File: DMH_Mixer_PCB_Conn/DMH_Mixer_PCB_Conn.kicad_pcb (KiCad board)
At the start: 2 copper layers, 48 x 43 mm, 8 parts, among them J1 TS_Jack_6.35mm_Sw, J2 TS_Jack_6.35mm_Sw, J3 TS_Jack_6.35mm_Sw, J4 TS_Jack_6.35mm_Sw, J5 TS_Jack_6.35mm_Sw, J50 Conn_01x08, J6 TS_Jack_6.35mm_Sw, J60 Conn_01x08

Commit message: Adapted connectors PCB to 4 channel
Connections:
- net /Core Circuit/Clipped Output renamed /Inputs and Outputs/Clipped Output Jack
- net /Core Circuit/Input 1 renamed /Inputs and Outputs/Input 1 Jack
- net /Core Circuit/Input 2 renamed /Inputs and Outputs/Input 2 Jack
- net /Core Circuit/Input 3 renamed /Inputs and Outputs/Input 3 Jack
- net /Core Circuit/Output + renamed /Inputs and Outputs/Input 4 Jack
- net /Core Circuit/Output - renamed /Inputs and Outputs/Output Jack

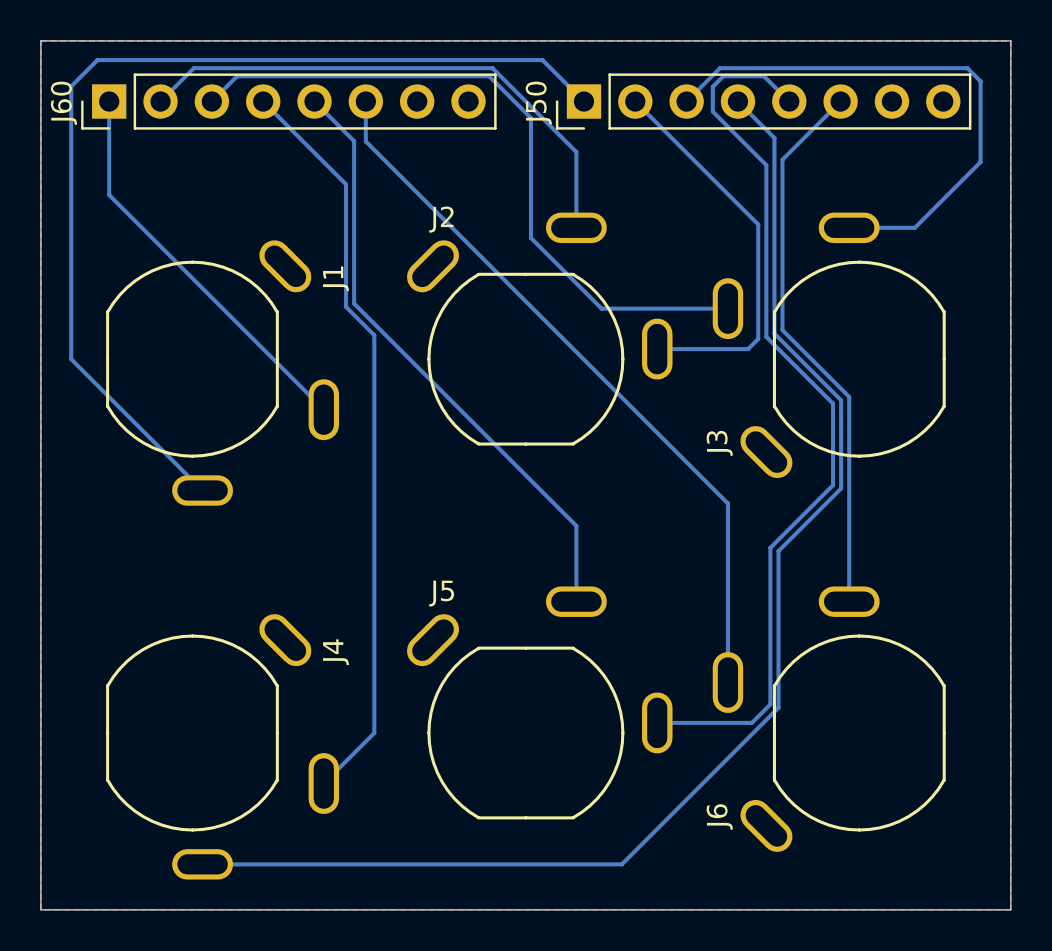
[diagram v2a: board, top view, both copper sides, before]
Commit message: Moved output jacks to bottom right
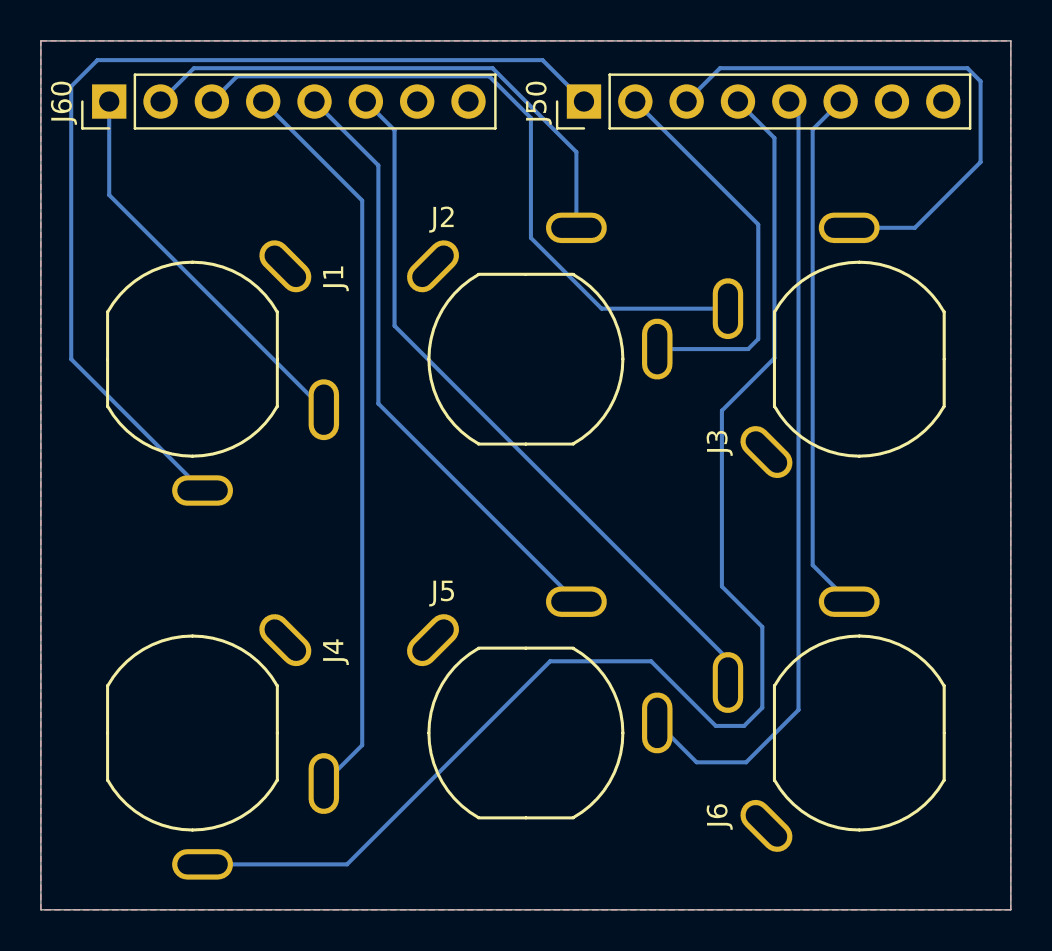
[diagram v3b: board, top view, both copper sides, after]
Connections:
- J4 pad T: /Inputs and Outputs/Clipped Output Jack -> /Inputs and Outputs/Input 4 Jack
- J5 pad T: /Inputs and Outputs/Output Jack -> /Inputs and Outputs/Clipped Output Jack
- J50 pad 4: /Inputs and Outputs/Clipped Output Jack -> /Inputs and Outputs/Input 4 Jack
- J50 pad 5: /Inputs and Outputs/Output Jack -> /Inputs and Outputs/Clipped Output Jack
- J50 pad 6: /Inputs and Outputs/Input 4 Jack -> /Inputs and Outputs/Output Jack
- J6 pad T: /Inputs and Outputs/Input 4 Jack -> /Inputs and Outputs/Output Jack
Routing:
- net /Inputs and Outputs/Input 4 Jack: track 27.3 -> 66.6 mm
- net /Inputs and Outputs/Clipped Output Jack: track 65.5 -> 39.4 mm
- net /Inputs and Outputs/Output Jack: track 45.1 -> 26.1 mm
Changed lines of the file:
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@@
 			(layers "*.Cu" "*.Mask")
 			(remove_unused_layers no)
-			(net 11 "/Inputs and Outputs/Clipped Output Jack")
+			(net 13 "/Inputs and Outputs/Input 4 Jack")
 			(pinfunction "Pin_4")
 			(pintype "passive")
@@
 			(layers "*.Cu" "*.Mask")
 			(remove_unused_layers no)
-			(net 12 "/Inputs and Outputs/Output Jack")
+			(net 11 "/Inputs and Outputs/Clipped Output Jack")
 			(pinfunction "Pin_5")
 			(pintype "passive")
@@
 			(layers "*.Cu" "*.Mask")
 			(remove_unused_layers no)
-			(net 13 "/Inputs and Outputs/Input 4 Jack")
+			(net 12 "/Inputs and Outputs/Output Jack")
 			(pinfunction "Pin_6")
 			(pintype "passive")
@@
 			)
 		)
-		(property "Function" "Clip"
+		(property "Function" "In 4"
 			(at 0 0 0)
 			(layer "B.SilkS")
@@
 			(layers "*.Cu" "*.Mask")
 			(remove_unused_layers no)
-			(net 11 "/Inputs and Outputs/Clipped Output Jack")
+			(net 13 "/Inputs and Outputs/Input 4 Jack")
 			(pintype "passive")
 			(solder_mask_margin 0.102)
@@
 			)
 		)
-		(property "Function" "In 4"
+		(property "Function" "Out"
 			(at 0 0 180)
 			(layer "B.SilkS")
@@
 			(layers "*.Cu" "*.Mask")
 			(remove_unused_layers no)
-			(net 13 "/Inputs and Outputs/Input 4 Jack")
+			(net 12 "/Inputs and Outputs/Output Jack")
 			(pintype "passive")
 			(solder_mask_margin 0.102)
@@
 			)
 		)
-		(property "Function" "Out"
+		(property "Function" "Clip"
 			(at 0 0 0)
 			(layer "B.SilkS")
@@
 			(layers "*.Cu" "*.Mask")
 			(remove_unused_layers no)
-			(net 12 "/Inputs and Outputs/Output Jack")
+			(net 11 "/Inputs and Outputs/Clipped Output Jack")
 			(pintype "passive")
 			(solder_mask_margin 0.102)
@@
 	)
 	(segment
-		(start 67.5 208.75)
-		(end 65 211.25)
-		(width 0.2)
-		(layer "B.Cu")
-		(net 5)
-	)
-	(segment
-		(start 66.1 181.6)
-		(end 66.1 187.665686)
-		(width 0.2)
-		(layer "B.Cu")
-		(net 5)
-	)
-	(segment
-		(start 66.1 187.665686)
-		(end 67.5 189.065686)
+		(start 62 177.5)
+		(end 66.9 182.4)
 		(width 0.2)
 		(layer "B.Cu")
@@
 	)
 	(segment
-		(start 67.5 189.065686)
-		(end 67.5 208.75)
+		(start 66.9 209.35)
+		(end 65 211.25)
 		(width 0.2)
 		(layer "B.Cu")
@@
 	)
 	(segment
-		(start 62 177.5)
-		(end 66.1 181.6)
+		(start 66.9 182.4)
+		(end 66.9 209.35)
 		(width 0.2)
 		(layer "B.Cu")
@@
 	)
 	(segment
-		(start 77.5 198.5)
-		(end 77.5 202.25)
+		(start 67.7 180.66)
+		(end 67.7 192.45)
 		(width 0.2)
 		(layer "B.Cu")
@@
 	)
 	(segment
-		(start 66.5 179.46)
-		(end 66.5 187.5)
+		(start 64.54 177.5)
+		(end 67.7 180.66)
 		(width 0.2)
 		(layer "B.Cu")
@@
 	)
 	(segment
-		(start 64.54 177.5)
-		(end 66.5 179.46)
+		(start 67.7 192.45)
+		(end 77.5 202.25)
 		(width 0.2)
 		(layer "B.Cu")
@@
 	)
 	(segment
-		(start 66.5 187.5)
-		(end 77.5 198.5)
+		(start 85 205.1)
+		(end 85 206.25)
 		(width 0.2)
 		(layer "B.Cu")
-		(net 6)
+		(net 7)
 	)
 	(segment
-		(start 85 197.394314)
-		(end 85 206.25)
+		(start 68.5 188.6)
+		(end 85 205.1)
 		(width 0.2)
 		(layer "B.Cu")
@@
 	)
 	(segment
-		(start 67.08 179.474314)
-		(end 85 197.394314)
+		(start 67.08 177.5)
+		(end 68.5 178.92)
 		(width 0.2)
 		(layer "B.Cu")
@@
 	)
 	(segment
-		(start 67.08 177.5)
-		(end 67.08 179.474314)
+		(start 68.5 178.92)
+		(end 68.5 188.6)
 		(width 0.2)
 		(layer "B.Cu")
@@
 	)
 	(segment
-		(start 85.495 177.065)
-		(end 85.495 177.5)
+		(start 88.31 177.5)
+		(end 88.035 177.5)
 		(width 0.2)
 		(layer "F.Cu")
@@
 	)
 	(segment
-		(start 90.6 196.65)
-		(end 87.5 199.75)
-		(width 0.2)
-		(layer "B.Cu")
-		(net 11)
-	)
-	(segment
-		(start 87.3 179.305)
-		(end 87.3 188.984314)
-		(width 0.2)
-		(layer "B.Cu")
-		(net 11)
-	)
-	(segment
-		(start 85.495 177.5)
-		(end 87.3 179.305)
+		(start 88.035 177.5)
+		(end 88.490969 177.955969)
 		(width 0.2)
 		(layer "B.Cu")
@@
 	)
 	(segment
-		(start 87.3 188.984314)
-		(end 90.6 192.284314)
+		(start 88.490969 177.955969)
+		(end 88.490969 207.609031)
 		(width 0.2)
 		(layer "B.Cu")
@@
 	)
 	(segment
-		(start 87.5 207.5)
-		(end 79.75 215.25)
+		(start 85.9 210.2)
+		(end 83.45 210.2)
 		(width 0.2)
 		(layer "B.Cu")
@@
 	)
 	(segment
-		(start 90.6 192.284314)
-		(end 90.6 196.65)
+		(start 88.490969 207.609031)
+		(end 85.9 210.2)
 		(width 0.2)
 		(layer "B.Cu")
@@
 	)
 	(segment
-		(start 87.5 199.75)
-		(end 87.5 207.5)
+		(start 83.45 210.2)
+		(end 81.5 208.25)
 		(width 0.2)
 		(layer "B.Cu")
@@
 	)
 	(segment
-		(start 79.75 215.25)
-		(end 59 215.25)
-		(width 0.2)
-		(layer "B.Cu")
-		(net 11)
-	)
-	(segment
-		(start 88.31 177.5)
-		(end 88.035 177.5)
-		(width 0.2)
-		(layer "F.Cu")
-		(net 12)
-	)
-	(segment
-		(start 90.2 196.484314)
-		(end 87.1 199.584314)
+		(start 89.192 178.883)
+		(end 89.192 200.442)
 		(width 0.2)
 		(layer "B.Cu")
@@
 	)
 	(segment
-		(start 88.035 177.5)
-		(end 86.785 176.25)
+		(start 90.575 177.5)
+		(end 89.192 178.883)
 		(width 0.2)
 		(layer "B.Cu")
@@
 	)
 	(segment
-		(start 86.9 180.65)
-		(end 86.9 189.15)
+		(start 89.192 200.442)
+		(end 91 202.25)
 		(width 0.2)
 		(layer "B.Cu")
@@
 	)
 	(segment
-		(start 86.9 189.15)
-		(end 90.2 192.45)
+		(start 85.495 177.065)
+		(end 85.495 177.5)
 		(width 0.2)
-		(layer "B.Cu")
-		(net 12)
+		(layer "F.Cu")
+		(net 13)
 	)
 	(segment
-		(start 84.770686 176.25)
-		(end 84.25 176.770686)
+		(start 87.3 179.305)
+		(end 87.3 190.2)
 		(width 0.2)
 		(layer "B.Cu")
-		(net 12)
+		(net 13)
 	)
 	(segment
-		(start 90.2 192.45)
-		(end 90.2 196.484314)
+		(start 85.8 208.4)
+		(end 84.4 208.4)
 		(width 0.2)
 		(layer "B.Cu")
-		(net 12)
+		(net 13)
 	)
 	(segment
-		(start 87.1 199.584314)
-		(end 87.1 207.334314)
+		(start 81.2 205.2)
+		(end 76.2 205.2)
 		(width 0.2)
 		(layer "B.Cu")
-		(net 12)
+		(net 13)
 	)
 	(segment
-		(start 84.25 176.770686)
-		(end 84.25 178)
+		(start 76.2 205.2)
+		(end 66.15 215.25)
 		(width 0.2)
 		(layer "B.Cu")
-		(net 12)
+		(net 13)
 	)
 	(segment
-		(start 86.184314 208.25)
-		(end 81.5 208.25)
+		(start 84.4 208.4)
+		(end 81.2 205.2)
 		(width 0.2)
 		(layer "B.Cu")
-		(net 12)
+		(net 13)
 	)
 	(segment
-		(start 86.785 176.25)
-		(end 84.770686 176.25)
+		(start 85.495 177.5)
+		(end 87.3 179.305)
 		(width 0.2)
 		(layer "B.Cu")
-		(net 12)
+		(net 13)
 	)
 	(segment
-		(start 84.25 178)
-		(end 86.9 180.65)
+		(start 66.15 215.25)
+		(end 59 215.25)
 		(width 0.2)
 		(layer "B.Cu")
-		(net 12)
+		(net 13)
 	)
 	(segment
-		(start 87.1 207.334314)
-		(end 86.184314 208.25)
+		(start 84.7 192.8)
+		(end 84.7 201.5)
 		(width 0.2)
 		(layer "B.Cu")
-		(net 12)
+		(net 13)
 	)
 	(segment
-		(start 87.7 188.818628)
-		(end 91 192.118628)
+		(start 86.7 207.5)
+		(end 85.8 208.4)
 		(width 0.2)
 		(layer "B.Cu")
@@
 	)
 	(segment
-		(start 91 192.118628)
-		(end 91 202.25)
+		(start 86.7 203.5)
+		(end 86.7 207.5)
 		(width 0.2)
 		(layer "B.Cu")
@@
 	)
 	(segment
-		(start 87.7 180.375)
-		(end 87.7 188.818628)
+		(start 84.7 201.5)
+		(end 86.7 203.5)
 		(width 0.2)
 		(layer "B.Cu")
@@
 	)
 	(segment
-		(start 90.575 177.5)
-		(end 87.7 180.375)
+		(start 87.3 190.2)
+		(end 84.7 192.8)
 		(width 0.2)
 		(layer "B.Cu")

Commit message: Panel and Connectors PCB ready
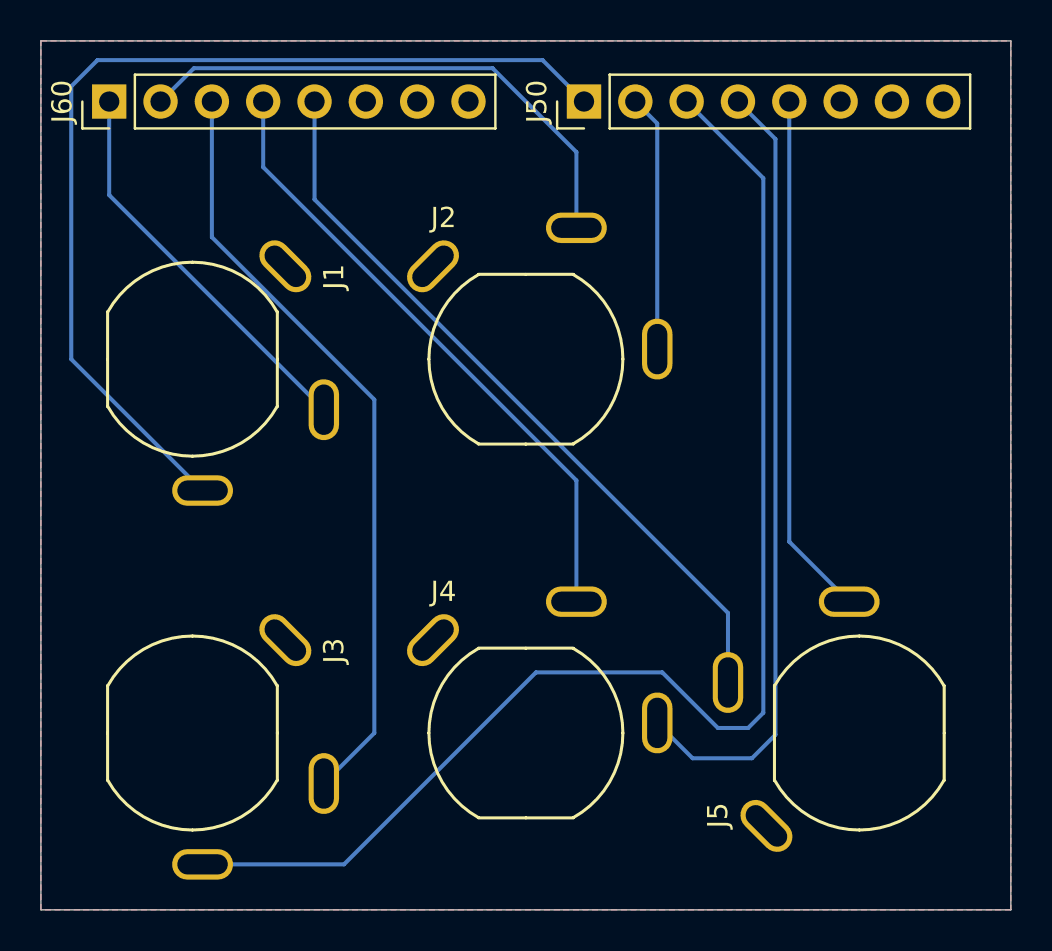
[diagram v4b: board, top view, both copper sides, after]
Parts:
- removed J6: TS_Jack_6.35mm_Sw, SynthStuff:CUI_MJ-63052A
- moved J3 37.8 mm to (58.5, 208.8), turned to -90 degrees
- moved J4 16.5 mm to (75.0, 208.8), turned to 0 degrees
- moved J5 16.5 mm to (91.5, 208.8), turned to 90 degrees
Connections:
- J5 pad T: /Inputs and Outputs/Clipped Output Jack -> /Inputs and Outputs/Output Jack
- J50 pad 5: /Inputs and Outputs/Clipped Output Jack -> /Inputs and Outputs/Output Jack
- J50 pad 6: /Inputs and Outputs/Output Jack -> unconnected-(J50-Pin_6-Pad6)
- J60 pad 6: Net-(J60-Pin_6) -> unconnected-(J60-Pin_6-Pad6)
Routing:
- net /Inputs and Outputs/Clipped Output Jack: track 39.4 -> 0.00 mm
- net /Inputs and Outputs/Input 3 Jack: track 27.3 -> 65.0 mm
- net Net-(J60-Pin_6): track 36.2 -> 0.00 mm
- net /Inputs and Outputs/Input 4 Jack: track 66.6 -> 39.6 mm
- net Net-(J60-Pin_5): track 30.1 -> 37.2 mm
- net /Inputs and Outputs/Input 2 Jack: track 19.6 -> 12.8 mm
- net Net-(J60-Pin_4): track 36.6 -> 31.2 mm
- net Net-(J60-Pin_3): track 34.3 -> 38.1 mm

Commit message: Prepared Gerbers for production
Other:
- board text added: "Mk1.0 - December 2024"
- board text removed: "Mk1.0 - Month Year"
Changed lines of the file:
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@@
 			(plot_on_all_layers_selection 0x0000000_00000000)
 			(disableapertmacros no)
-			(usegerberextensions no)
+			(usegerberextensions yes)
 			(usegerberattributes yes)
 			(usegerberadvancedattributes yes)
@@
 			(plotinvisibletext no)
 			(sketchpadsonfab no)
-			(subtractmaskfromsilk no)
+			(subtractmaskfromsilk yes)
 			(outputformat 1)
 			(mirror no)
-			(drillshape 1)
+			(drillshape 0)
 			(scaleselection 1)
-			(outputdirectory "")
+			(outputdirectory "Gerbers/")
 		)
 	)
@@
 		)
 		(property "Function" "In 3"
-			(at 0 0 360)
+			(at 0 0 0)
 			(layer "B.SilkS")
 			(effects
@@
 		)
 		(property "Function" "Out"
-			(at 0 0 360)
+			(at 0 0 0)
 			(layer "B.SilkS")
 			(effects
@@
 		(layer "User.9")
 	)
-	(gr_text "Mk1.0 - Month Year"
+	(gr_text "Mk1.0 - December 2024"
 		(at 74.75 216.25 0)
 		(layer "B.SilkS")
